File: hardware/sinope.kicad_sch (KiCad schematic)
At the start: 33 parts, among them J1 SERIAL0, J2 PIOA, J3 SERIAL1, J4 PIOB, SW1 RESET, U1 Z80CTC, U10 74LS74, U2 Z80SIO, U3 Z80PIO, U4 Z80CPU, U5 74LS138, U6 65256, U7 27256, U8 74LS04, U9 74LS32, Y1 6.5Mhz

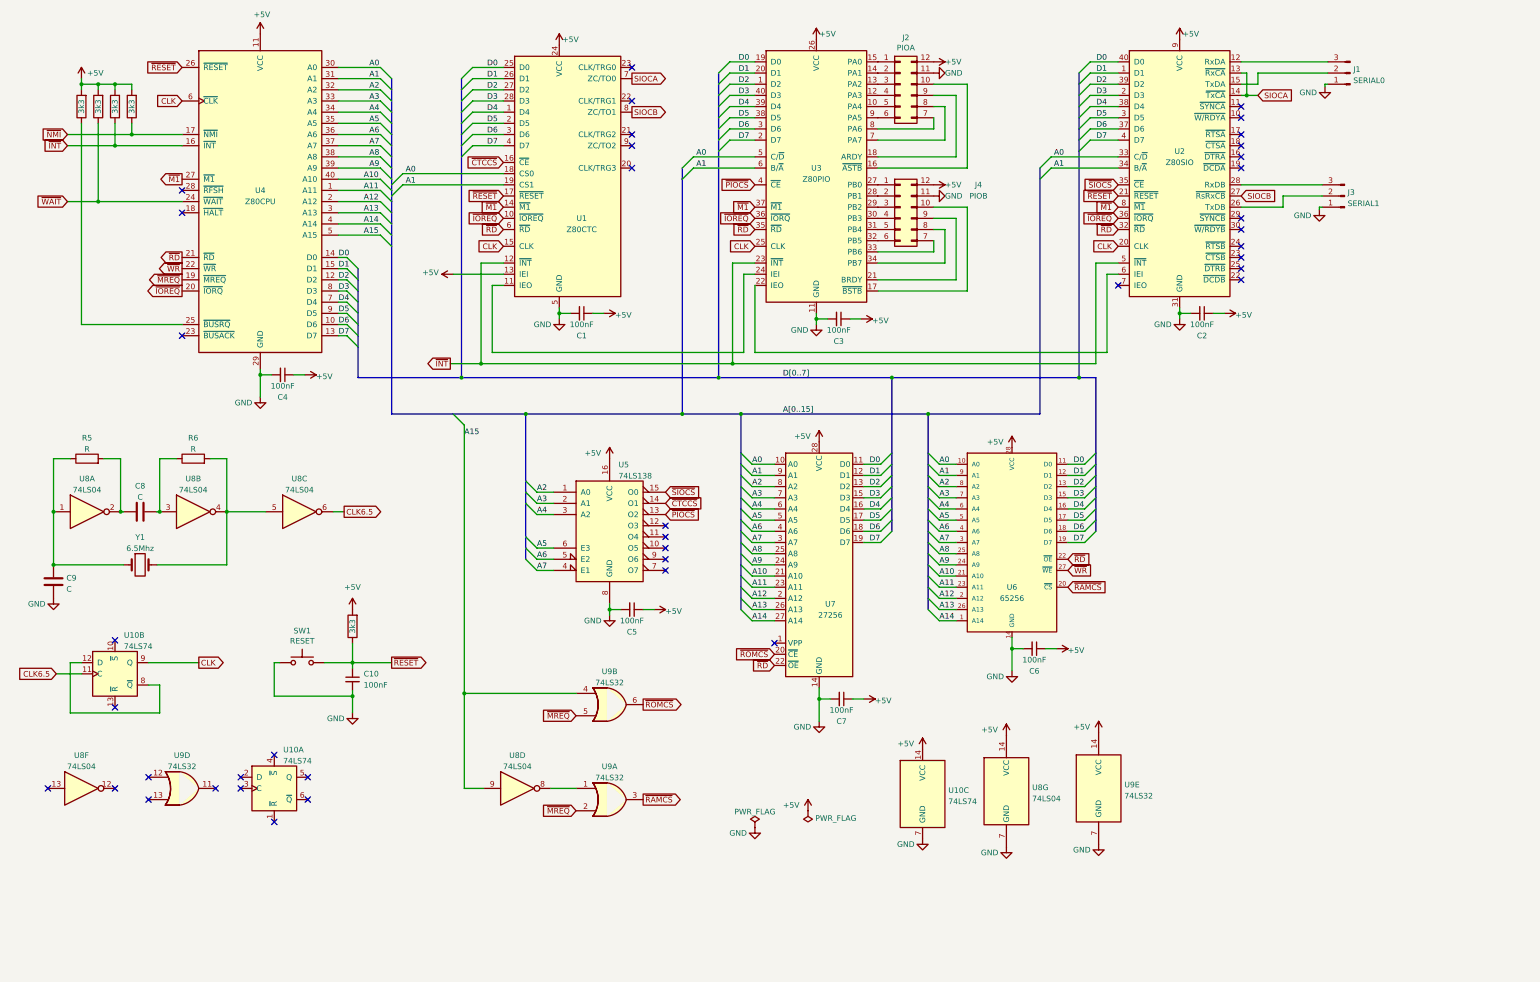
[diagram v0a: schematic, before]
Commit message: Make it match the actual build
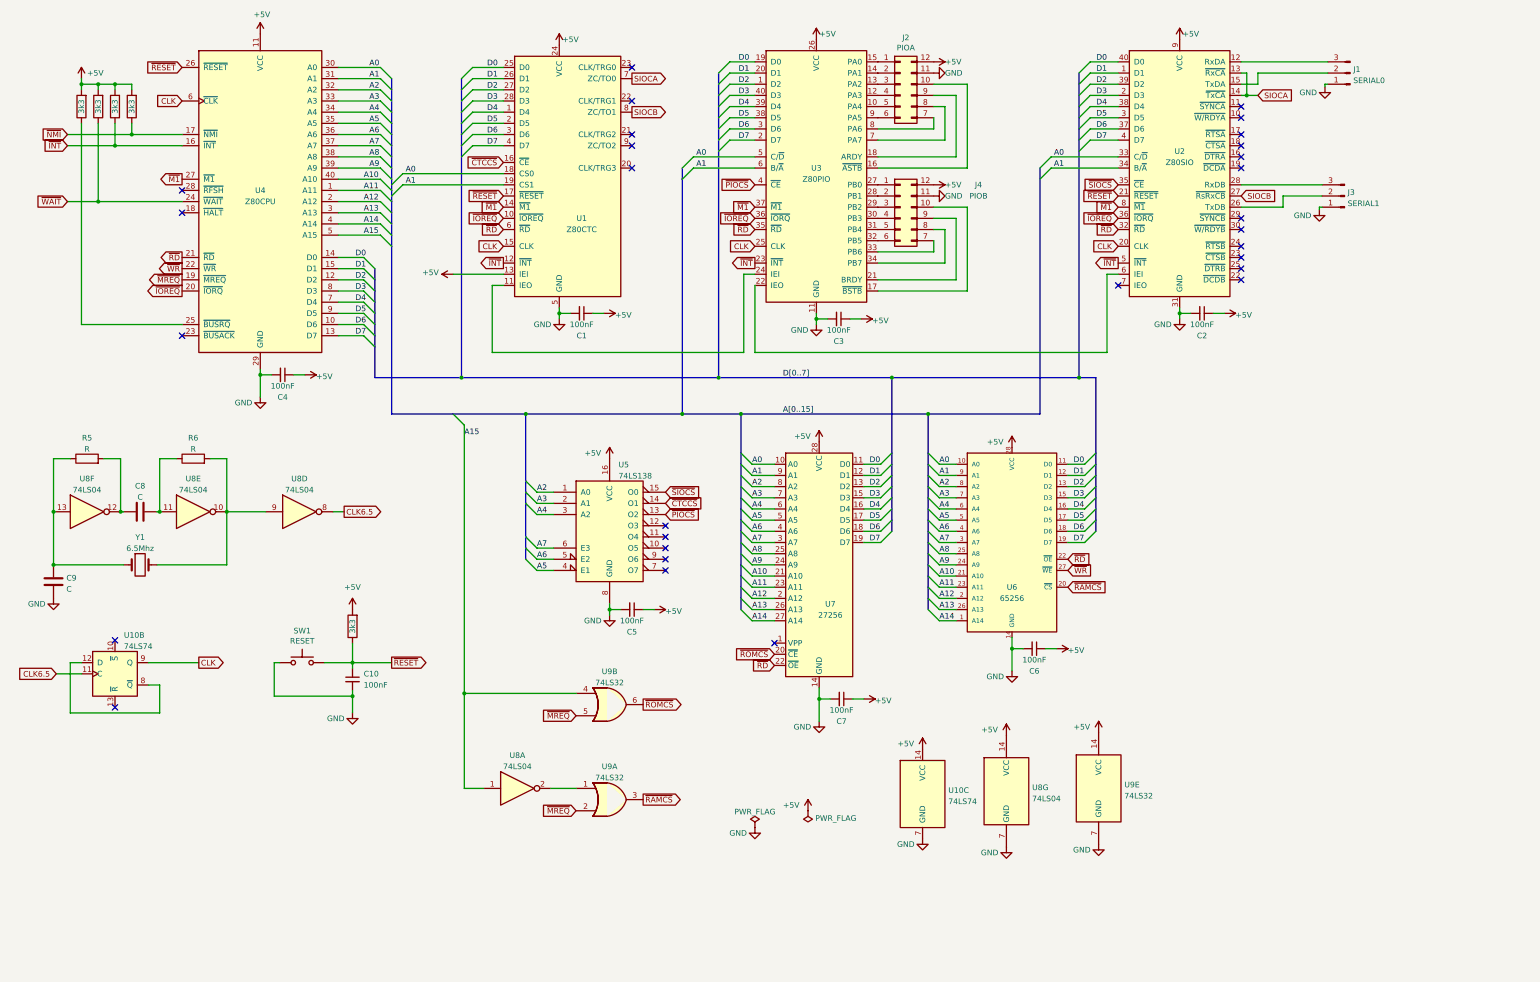
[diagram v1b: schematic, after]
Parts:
- removed unit 1 of U10
- removed unit 3 of U8
- removed unit 2 of U8
- removed unit 4 of U9
- added unit 5 of U8
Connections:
- net A15: now also U8.1; no longer U8.9
- net A5: now also U5.4 (E1); no longer U5.6 (E3)
- net A7: now also U5.6 (E3); no longer U5.4 (E1)
- net CLK6.5: now also U8.8
- net at U9.1: now also U8.2; no longer U8.8
- net at C9.2, R5.1, Y1.1: now also U8.13; no longer U8.1
- net at C8.1, R5.2: now also U8.12; no longer U8.2
- net at C8.2, R6.1: now also U8.11
- net at R6.2, Y1.2: now also U8.9, U8.10
- no-connect marks 40 -> 29
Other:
- moved on the sheet: U8A, U8D, U8F

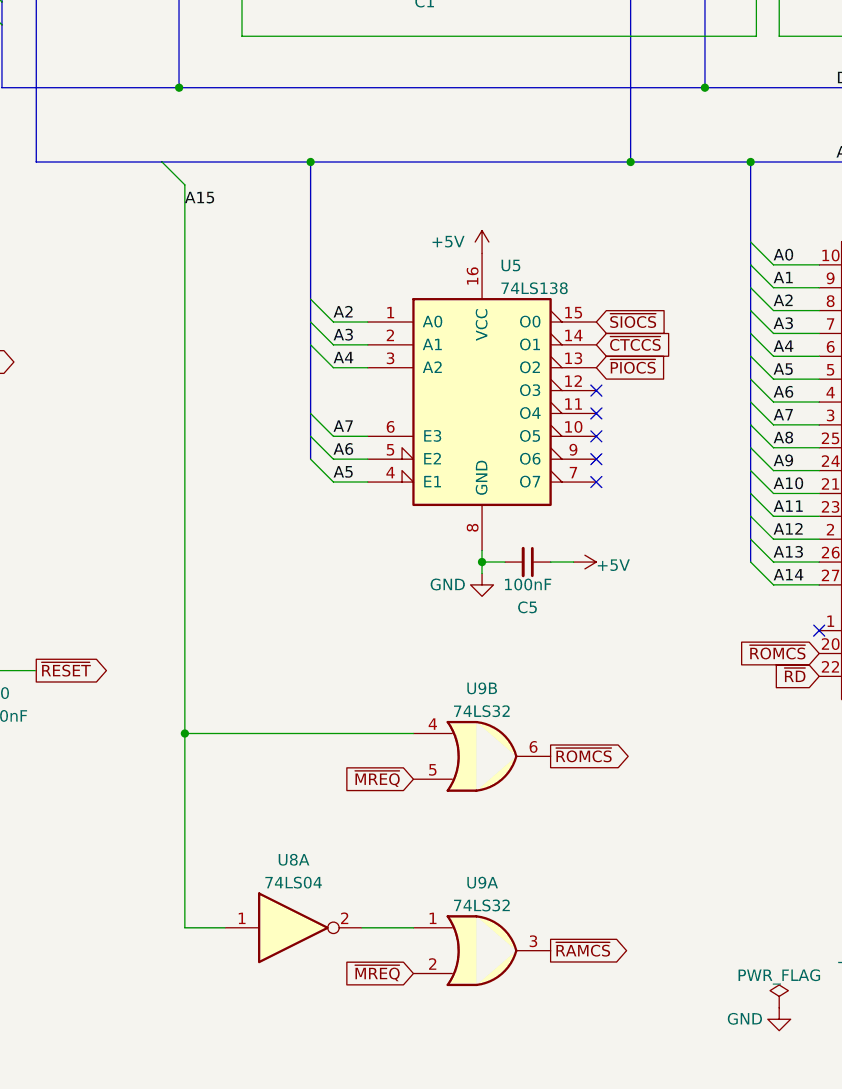
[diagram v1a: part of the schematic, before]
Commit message: Add hardware test program
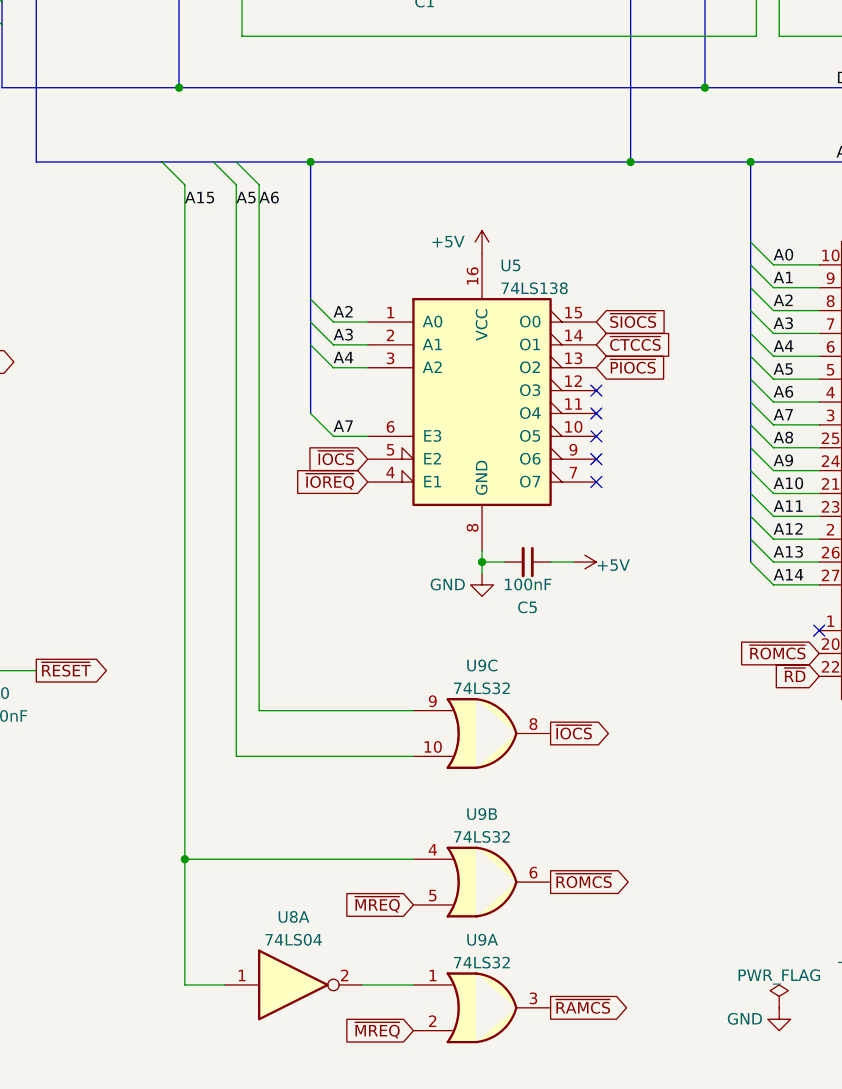
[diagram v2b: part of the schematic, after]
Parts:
- added unit 3 of U9
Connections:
- net A5: now also U9.10; no longer U5.4 (E1)
- net A6: now also U9.9; no longer U5.5 (E2)
- net ~{IOREQ}: now also U5.4 (E1)
- new net ~{IOCS}: U5.5 (E2), U9.8
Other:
- moved on the sheet: U8A, U9A, U9B

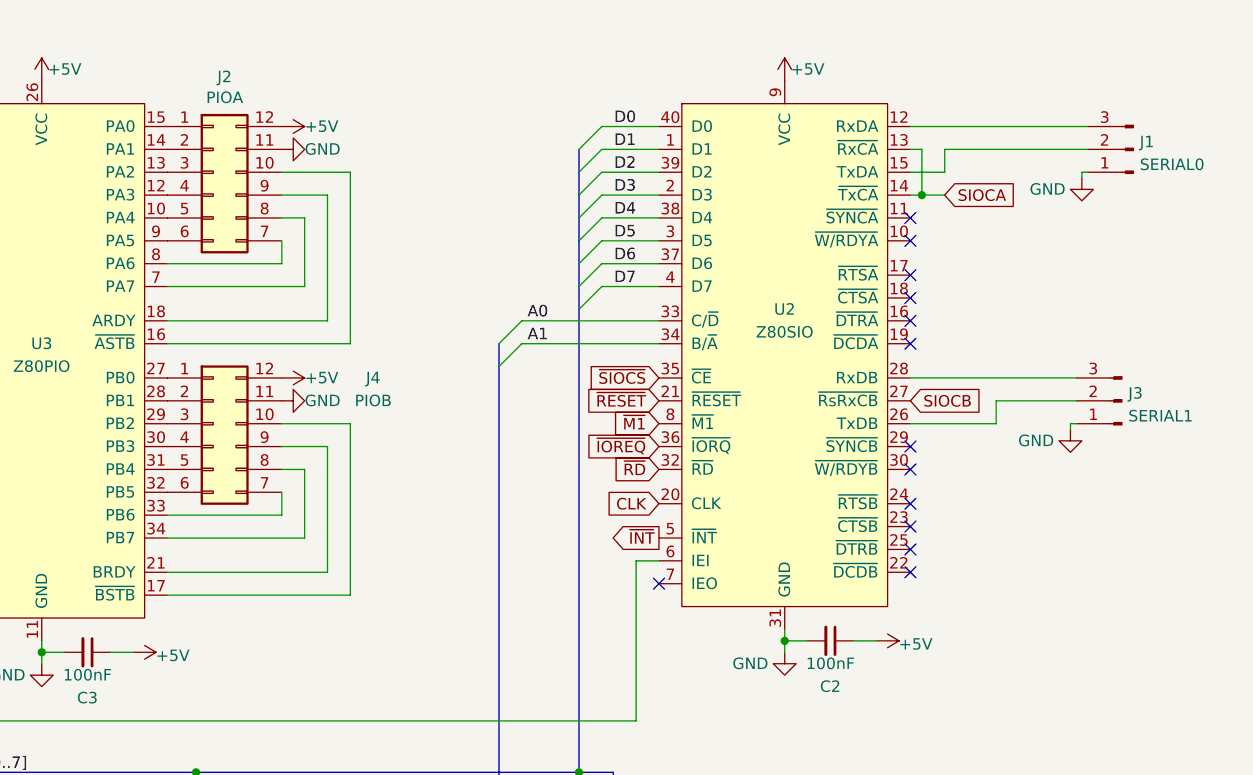
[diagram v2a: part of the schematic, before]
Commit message: Replace connectors to reflect reality
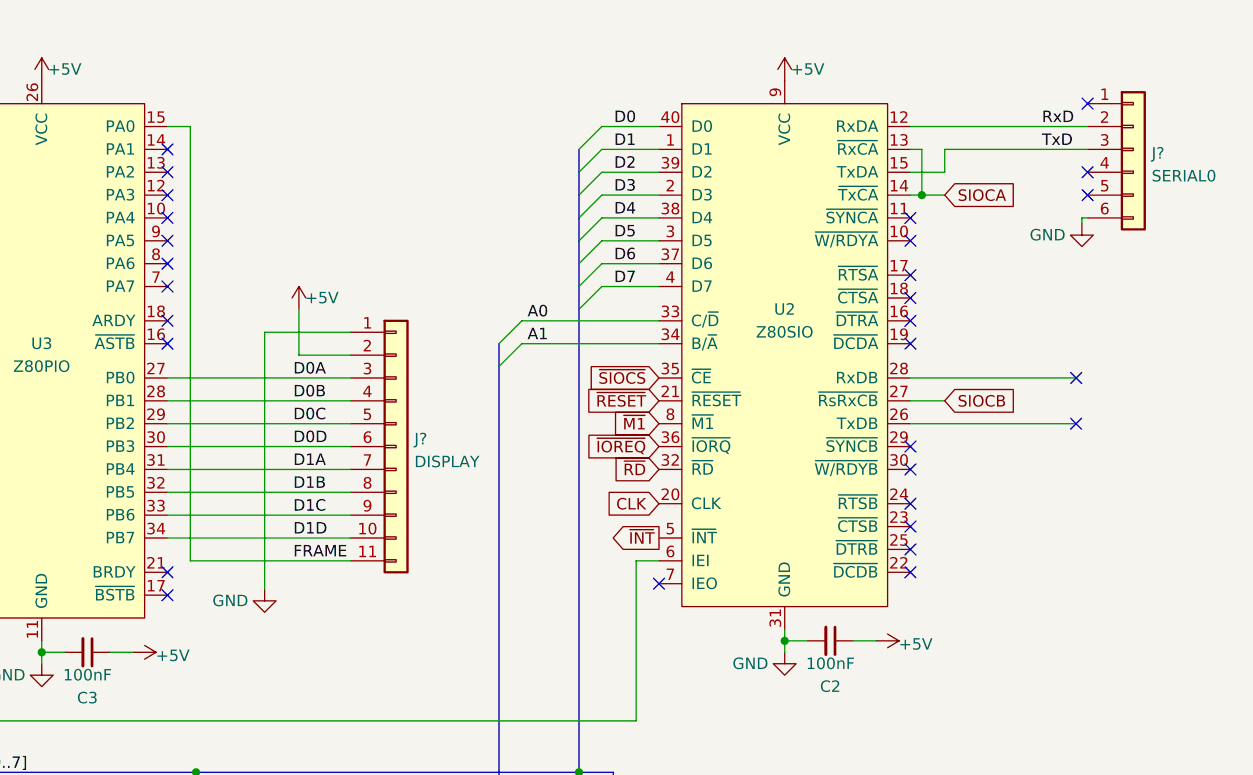
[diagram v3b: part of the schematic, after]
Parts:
- removed J1: SERIAL0, symbol Connector:Conn_01x03_Male
- removed J2: PIOA, Connector_PinHeader_2.54mm:PinHeader_2x06_P2.54mm_Vertical, symbol Connector_Generic:Conn_02x06_Counter_Clockwise
- removed J3: SERIAL1, symbol Connector:Conn_01x03_Male
- removed J4: PIOB, Connector_PinHeader_2.54mm:PinHeader_2x06_P2.54mm_Vertical, symbol Connector_Generic:Conn_02x06_Counter_Clockwise
- added J?: DISPLAY, symbol Connector_Generic:Conn_01x11
- added J?: SERIAL0, symbol Connector_Generic:Conn_01x06
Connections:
- net +5V: now also J?.2 (Pin_2)
- net GND: now also J?.1 (Pin_1), J?.6 (Pin_6)
- net RxD: now reaches U2.12 (RxDA)
- net RxD: now also J?.2 (Pin_2)
- net TxD: now reaches U2.15 (TxDA)
- net TxD: now also J?.3 (Pin_3)
- net FRAME: now reaches U3.15 (PA0)
- net FRAME: now also J?.11 (Pin_11)
- net D0A: now reaches U3.27 (PB0)
- net D0A: now also J?.3 (Pin_3)
- net D0B: now reaches U3.28 (PB1)
- net D0B: now also J?.4 (Pin_4)
- net D0C: now reaches U3.29 (PB2)
- net D0C: now also J?.5 (Pin_5)
- net D0D: now reaches U3.30 (PB3)
- net D0D: now also J?.6 (Pin_6)
- net D1A: now reaches U3.31 (PB4)
- net D1A: now also J?.7 (Pin_7)
- net D1B: now reaches U3.32 (PB5)
- net D1B: now also J?.8 (Pin_8)
- net D1C: now reaches U3.33 (PB6)
- net D1C: now also J?.9 (Pin_9)
- net D1D: now reaches U3.34 (PB7)
- net D1D: now also J?.10 (Pin_10)
- no-connect marks 29 -> 45
